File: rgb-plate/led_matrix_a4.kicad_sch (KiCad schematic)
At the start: 32 parts

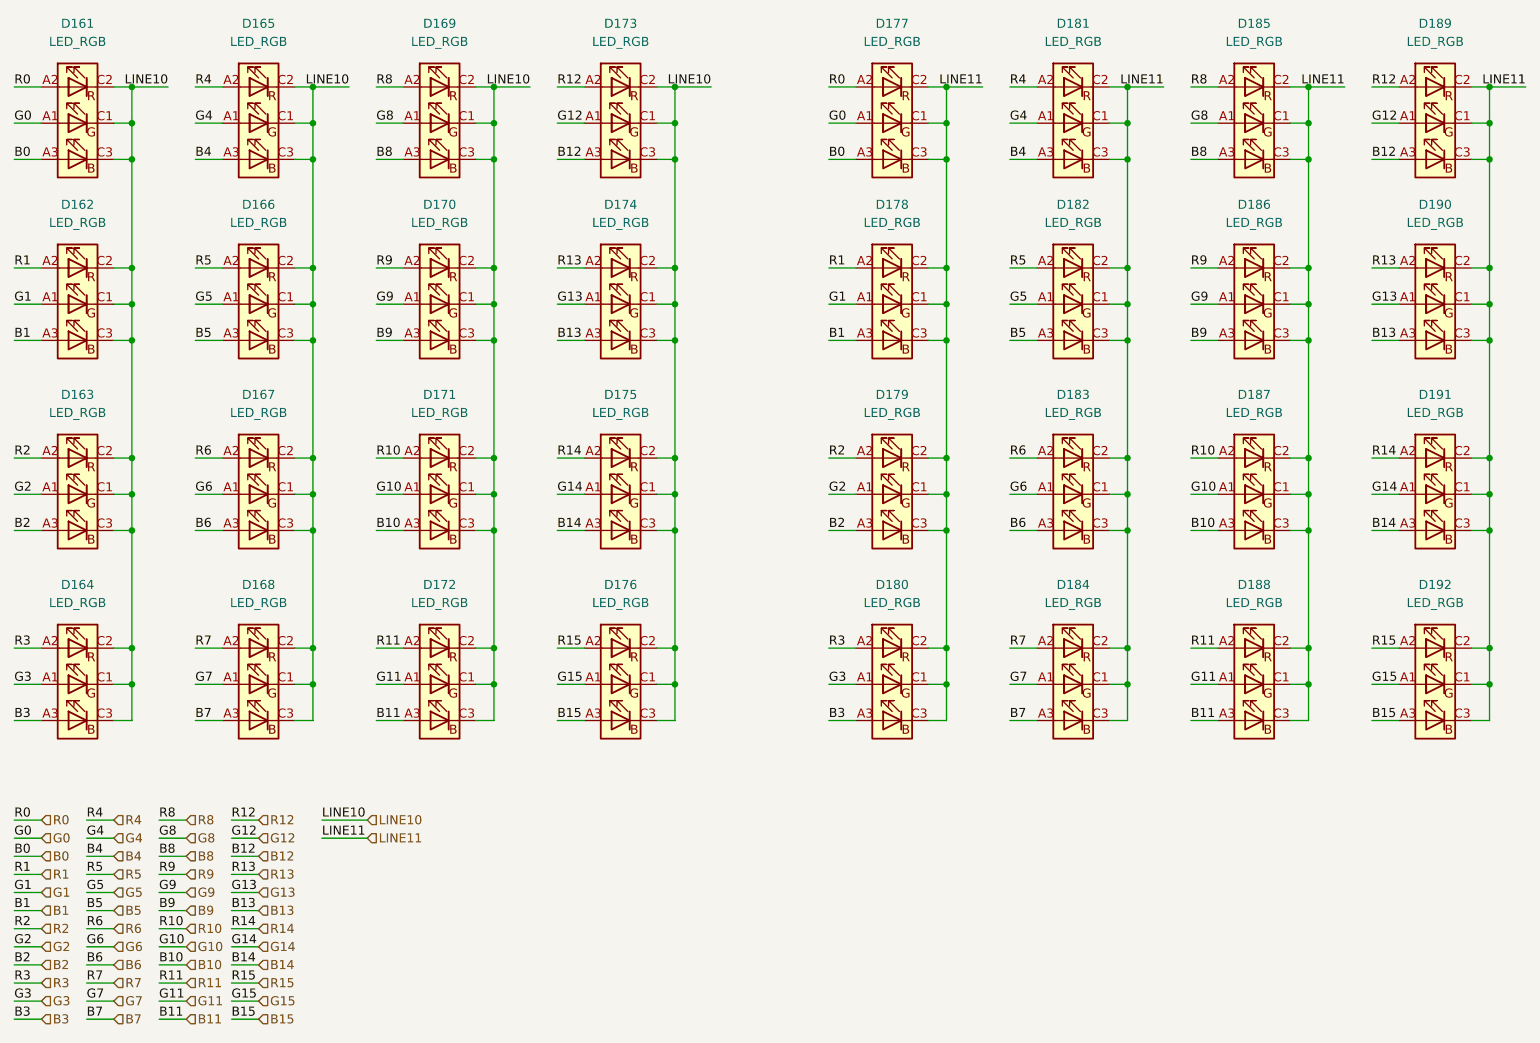
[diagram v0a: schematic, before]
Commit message: initial layout on single board, may need to split up
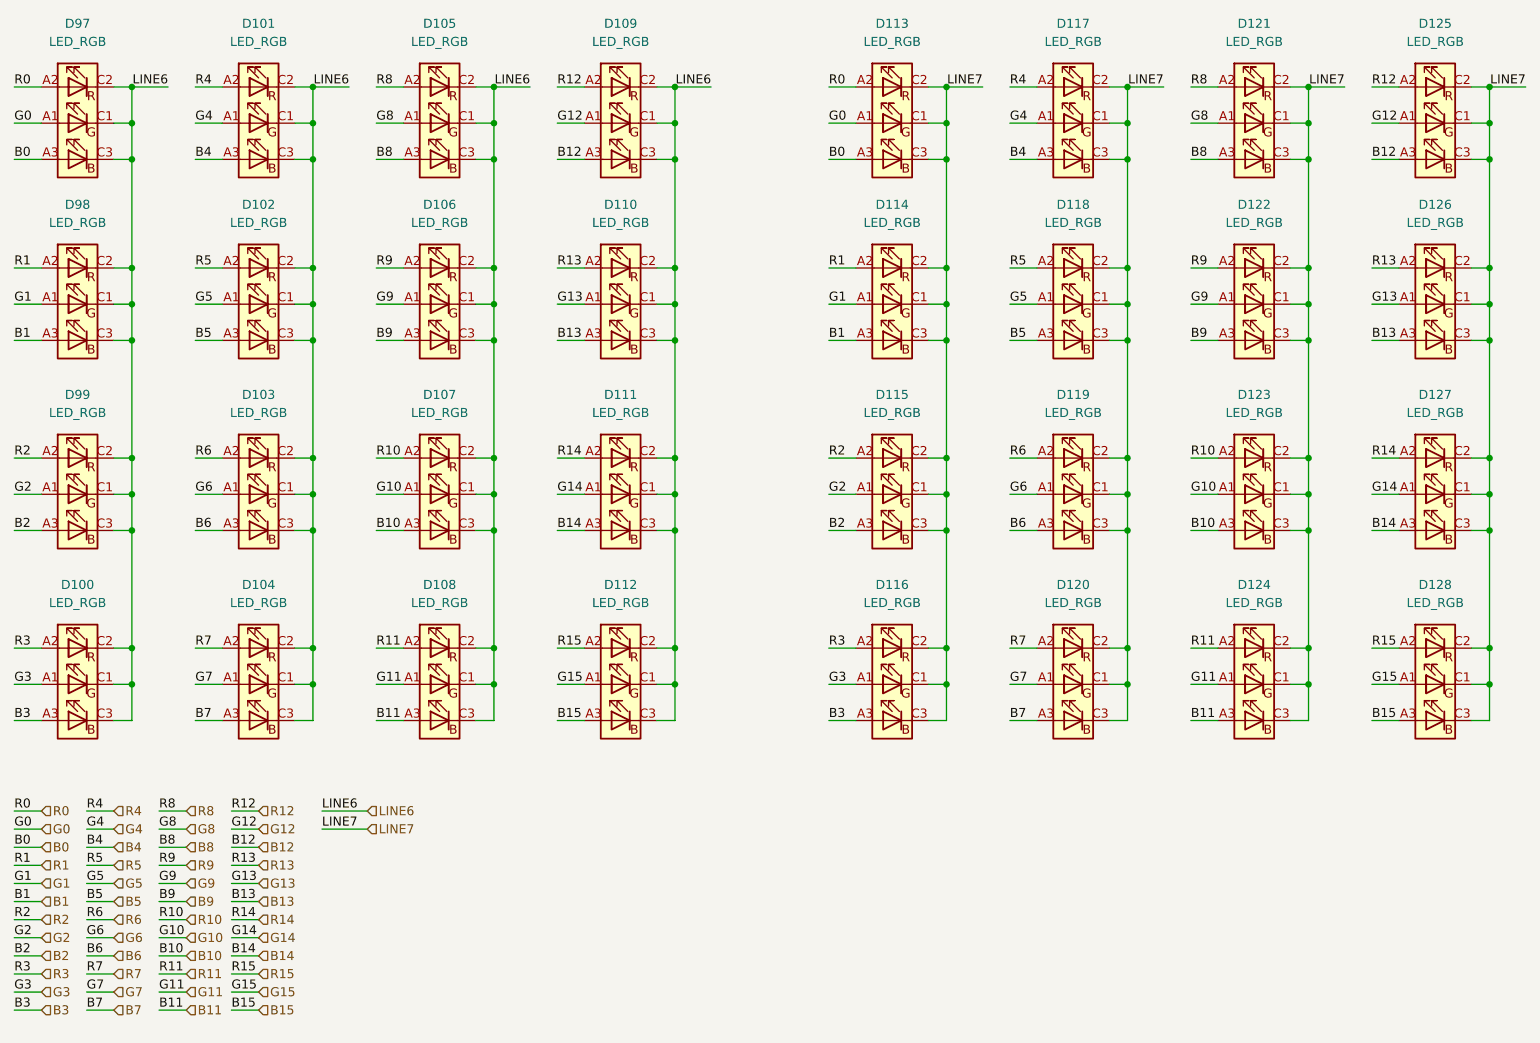
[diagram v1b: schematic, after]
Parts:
- removed D161, D162, D163, D164, D165, D166, D167, D168, D169, D170, D171, D172, D173, D174, D175, D176, D177, D178, D179, D180, D181, D182, D183, D184, D185, D186, D187, D188, D189, D190, D191, D192: LED_RGB, LRTBGVSR-4U4V-JW+8A8B-D8-3S4U-7Z:LRTBGVSR4U4VJW8A8BD83S4U7Z, symbol LRTBGVSR-4U4V-JW+8A8B-D8-3S4U-:LED_RGB
- added D100, D101, D102, D103, D104, D105, D106, D107, D108, D109, D110, D111, D112, D113, D114, D115, D116, D117, D118, D119, D120, D121, D122, D123, D124, D125, D126, D127, D128, D97, D98, D99: LED_RGB, LRTBGVSR-4U4V-JW+8A8B-D8-3S4U-7Z:LRTBGVSR4U4VJW8A8BD83S4U7Z, symbol LRTBGVSR-4U4V-JW+8A8B-D8-3S4U-:LED_RGB
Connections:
- net B0: now also D113.A3 (BA), D97.A3 (BA)
- net B1: now also D114.A3 (BA), D98.A3 (BA)
- net B10: now also D107.A3 (BA), D123.A3 (BA)
- net B11: now also D108.A3 (BA), D124.A3 (BA)
- net B12: now also D109.A3 (BA), D125.A3 (BA)
- net B13: now also D110.A3 (BA), D126.A3 (BA)
- net B14: now also D111.A3 (BA), D127.A3 (BA)
- net B15: now also D112.A3 (BA), D128.A3 (BA)
- net B2: now also D115.A3 (BA), D99.A3 (BA)
- net B3: now also D100.A3 (BA), D116.A3 (BA)
- net B4: now also D101.A3 (BA), D117.A3 (BA)
- net B5: now also D102.A3 (BA), D118.A3 (BA)
- net B6: now also D103.A3 (BA), D119.A3 (BA)
- net B7: now also D104.A3 (BA), D120.A3 (BA)
- net B8: now also D105.A3 (BA), D121.A3 (BA)
- net B9: now also D106.A3 (BA), D122.A3 (BA)
- net G0: now also D113.A1 (GA), D97.A1 (GA)
- net G1: now also D114.A1 (GA), D98.A1 (GA)
- net G10: now also D107.A1 (GA), D123.A1 (GA)
- net G11: now also D108.A1 (GA), D124.A1 (GA)
- net G12: now also D109.A1 (GA), D125.A1 (GA)
- net G13: now also D110.A1 (GA), D126.A1 (GA)
- net G14: now also D111.A1 (GA), D127.A1 (GA)
- net G15: now also D112.A1 (GA), D128.A1 (GA)
- net G2: now also D115.A1 (GA), D99.A1 (GA)
- net G3: now also D100.A1 (GA), D116.A1 (GA)
- net G4: now also D101.A1 (GA), D117.A1 (GA)
- net G5: now also D102.A1 (GA), D118.A1 (GA)
- net G6: now also D103.A1 (GA), D119.A1 (GA)
- net G7: now also D104.A1 (GA), D120.A1 (GA)
- net G8: now also D105.A1 (GA), D121.A1 (GA)
- net G9: now also D106.A1 (GA), D122.A1 (GA)
- net R0: now also D113.A2 (RA), D97.A2 (RA)
- net R1: now also D114.A2 (RA), D98.A2 (RA)
- net R10: now also D107.A2 (RA), D123.A2 (RA)
- net R11: now also D108.A2 (RA), D124.A2 (RA)
- net R12: now also D109.A2 (RA), D125.A2 (RA)
- net R13: now also D110.A2 (RA), D126.A2 (RA)
- net R14: now also D111.A2 (RA), D127.A2 (RA)
- net R15: now also D112.A2 (RA), D128.A2 (RA)
- net R2: now also D115.A2 (RA), D99.A2 (RA)
- net R3: now also D100.A2 (RA), D116.A2 (RA)
- net R4: now also D101.A2 (RA), D117.A2 (RA)
- net R5: now also D102.A2 (RA), D118.A2 (RA)
- net R6: now also D103.A2 (RA), D119.A2 (RA)
- net R7: now also D104.A2 (RA), D120.A2 (RA)
- net R8: now also D105.A2 (RA), D121.A2 (RA)
- net R9: now also D106.A2 (RA), D122.A2 (RA)
- new net LINE6: D100.C1 (GK), D100.C2 (RK), D100.C3 (BK), D101.C1 (GK), D101.C2 (RK), D101.C3 (BK), D102.C1 (GK), D102.C2 (RK), D102.C3 (BK), D103.C1 (GK), D103.C2 (RK), D103.C3 (BK), D104.C1 (GK), D104.C2 (RK), D104.C3 (BK), D105.C1 (GK), D105.C2 (RK), D105.C3 (BK), D106.C1 (GK), D106.C2 (RK), D106.C3 (BK), D107.C1 (GK), D107.C2 (RK), D107.C3 (BK), D108.C1 (GK), D108.C2 (RK), D108.C3 (BK), D109.C1 (GK), D109.C2 (RK), D109.C3 (BK), D110.C1 (GK), D110.C2 (RK), D110.C3 (BK), D111.C1 (GK), D111.C2 (RK), D111.C3 (BK), D112.C1 (GK), D112.C2 (RK), D112.C3 (BK), D97.C1 (GK), D97.C2 (RK), D97.C3 (BK), D98.C1 (GK), D98.C2 (RK), D98.C3 (BK), D99.C1 (GK), D99.C2 (RK), D99.C3 (BK)
- new net LINE7: D113.C1 (GK), D113.C2 (RK), D113.C3 (BK), D114.C1 (GK), D114.C2 (RK), D114.C3 (BK), D115.C1 (GK), D115.C2 (RK), D115.C3 (BK), D116.C1 (GK), D116.C2 (RK), D116.C3 (BK), D117.C1 (GK), D117.C2 (RK), D117.C3 (BK), D118.C1 (GK), D118.C2 (RK), D118.C3 (BK), D119.C1 (GK), D119.C2 (RK), D119.C3 (BK), D120.C1 (GK), D120.C2 (RK), D120.C3 (BK), D121.C1 (GK), D121.C2 (RK), D121.C3 (BK), D122.C1 (GK), D122.C2 (RK), D122.C3 (BK), D123.C1 (GK), D123.C2 (RK), D123.C3 (BK), D124.C1 (GK), D124.C2 (RK), D124.C3 (BK), D125.C1 (GK), D125.C2 (RK), D125.C3 (BK), D126.C1 (GK), D126.C2 (RK), D126.C3 (BK), D127.C1 (GK), D127.C2 (RK), D127.C3 (BK), D128.C1 (GK), D128.C2 (RK), D128.C3 (BK)
